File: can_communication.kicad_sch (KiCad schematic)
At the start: 22 parts, among them J6 Conn_01x03, J7 Conn_01x03, U11 SN65HVD230, U12 MCP2515-xSO, U13 SN65HVD230, Y3 16MHz

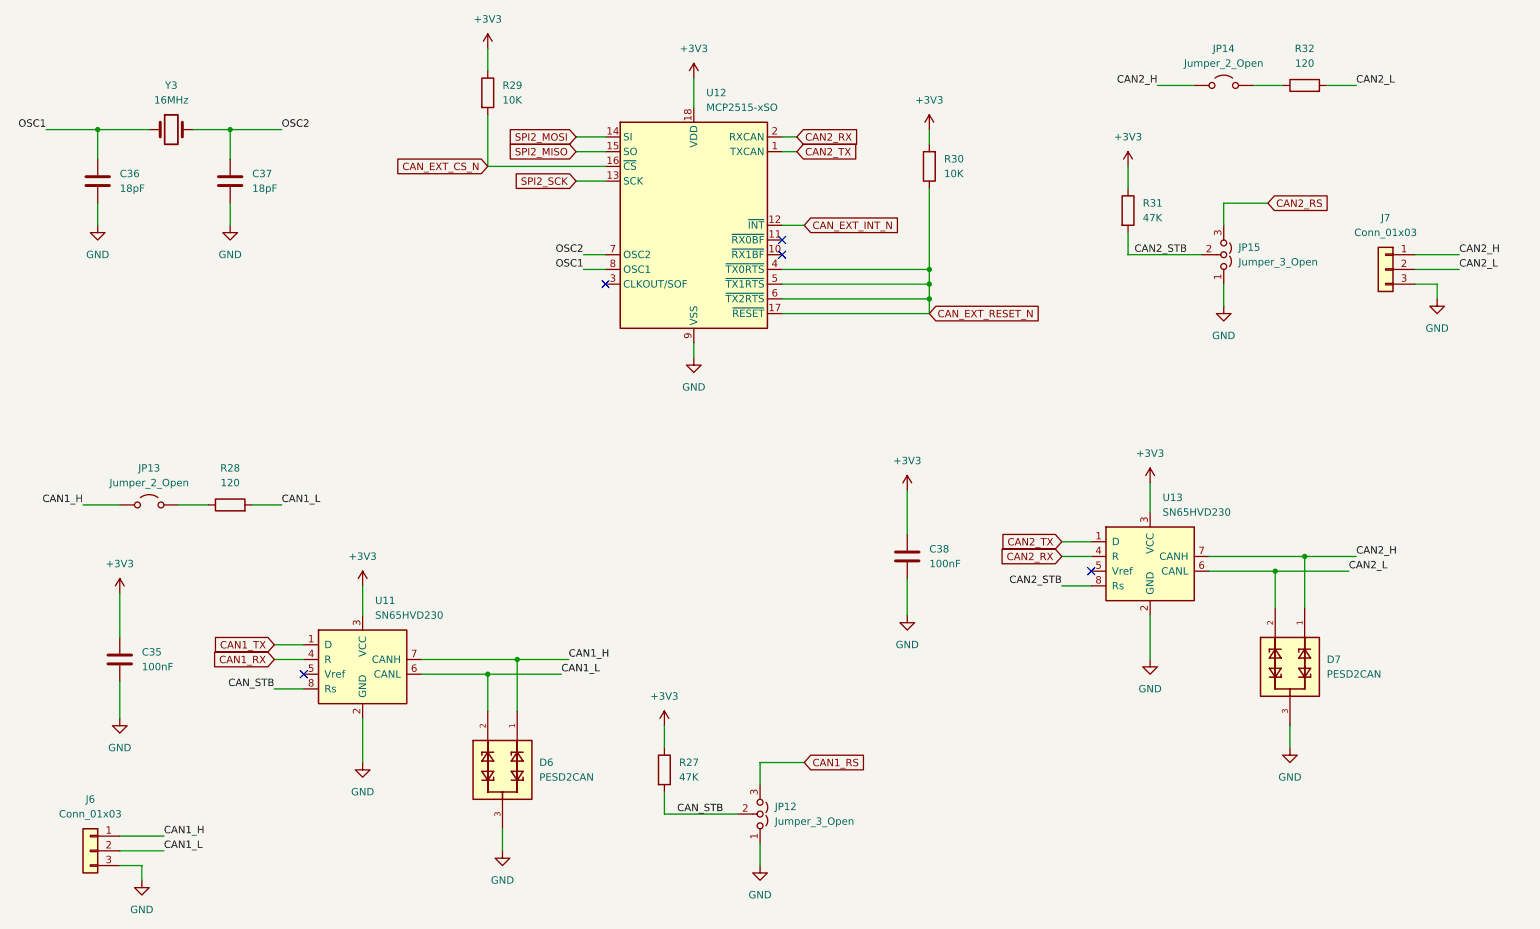
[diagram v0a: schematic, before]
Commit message: feat: implement analog and timer block
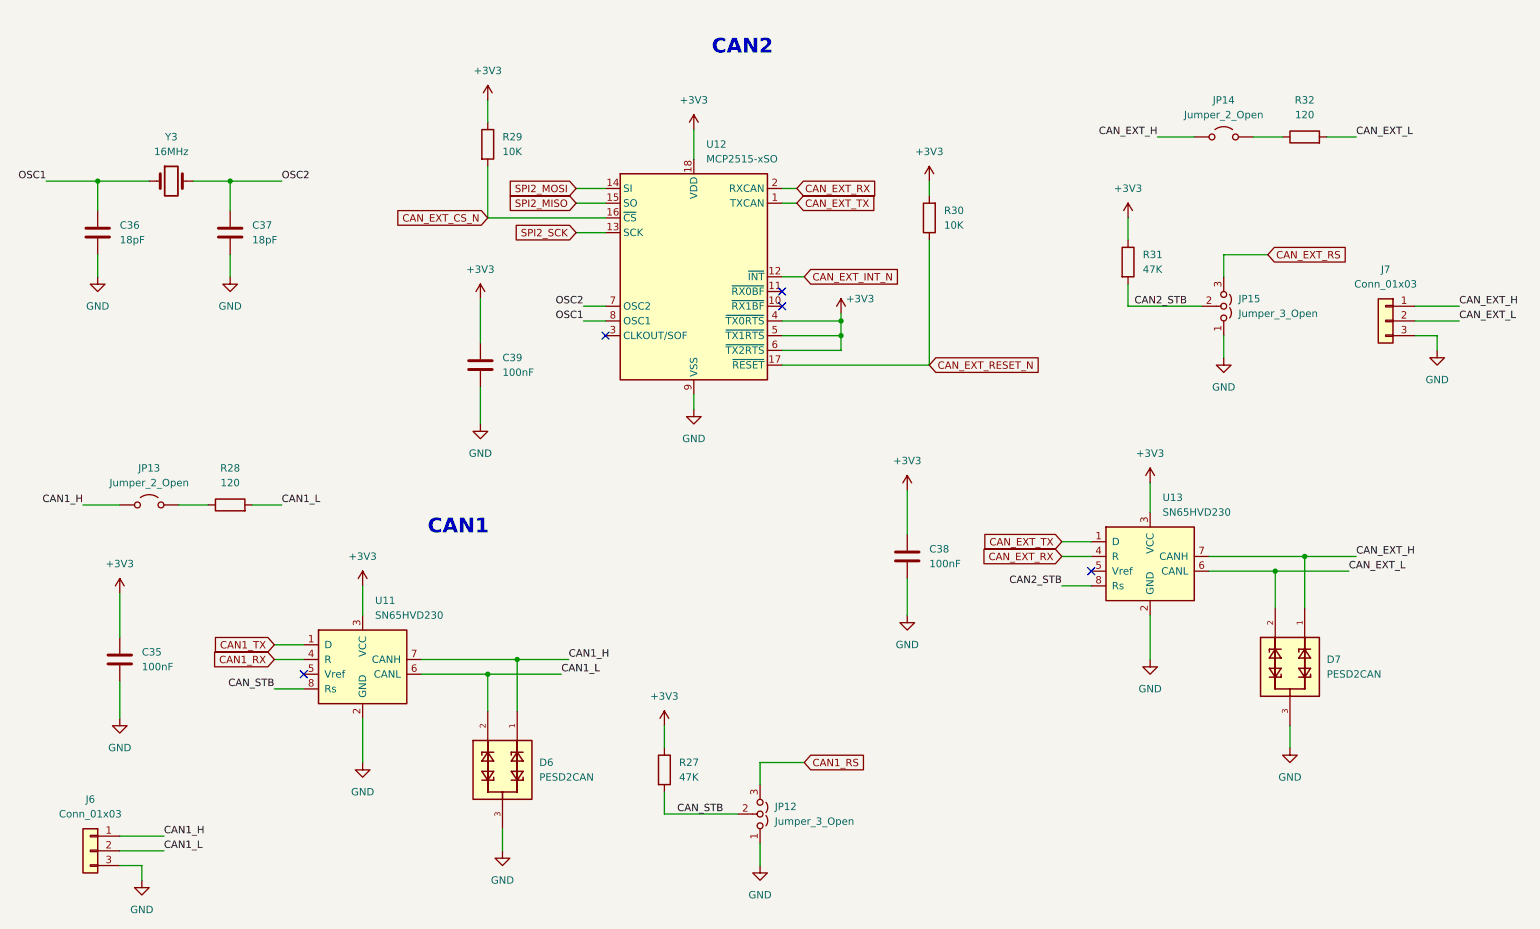
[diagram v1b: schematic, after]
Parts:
- added C39: 100nF, symbol Device:C
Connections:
- net +3V3: now also U12.4 (~{TX0RTS}), U12.5 (~{TX1RTS}), U12.6 (~{TX2RTS}), C39.1
- net CAN_EXT_RESET_N: no longer U12.4 (~{TX0RTS}), U12.5 (~{TX1RTS}), U12.6 (~{TX2RTS})
- net GND: now also C39.2
- net CAN2_H renamed CAN_EXT_H
- net CAN2_L renamed CAN_EXT_L
- net CAN2_RS renamed CAN_EXT_RS
- net CAN2_RX renamed CAN_EXT_RX
- net CAN2_TX renamed CAN_EXT_TX
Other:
- note added: "CAN1"
- note added: "CAN2"
- moved on the sheet: C36, C37, J7, JP14, JP15, R29, R30, R31, R32, U12, Y3
